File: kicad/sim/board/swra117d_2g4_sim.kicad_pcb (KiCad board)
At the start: 2 copper layers, 40 x 30 mm, 1 part

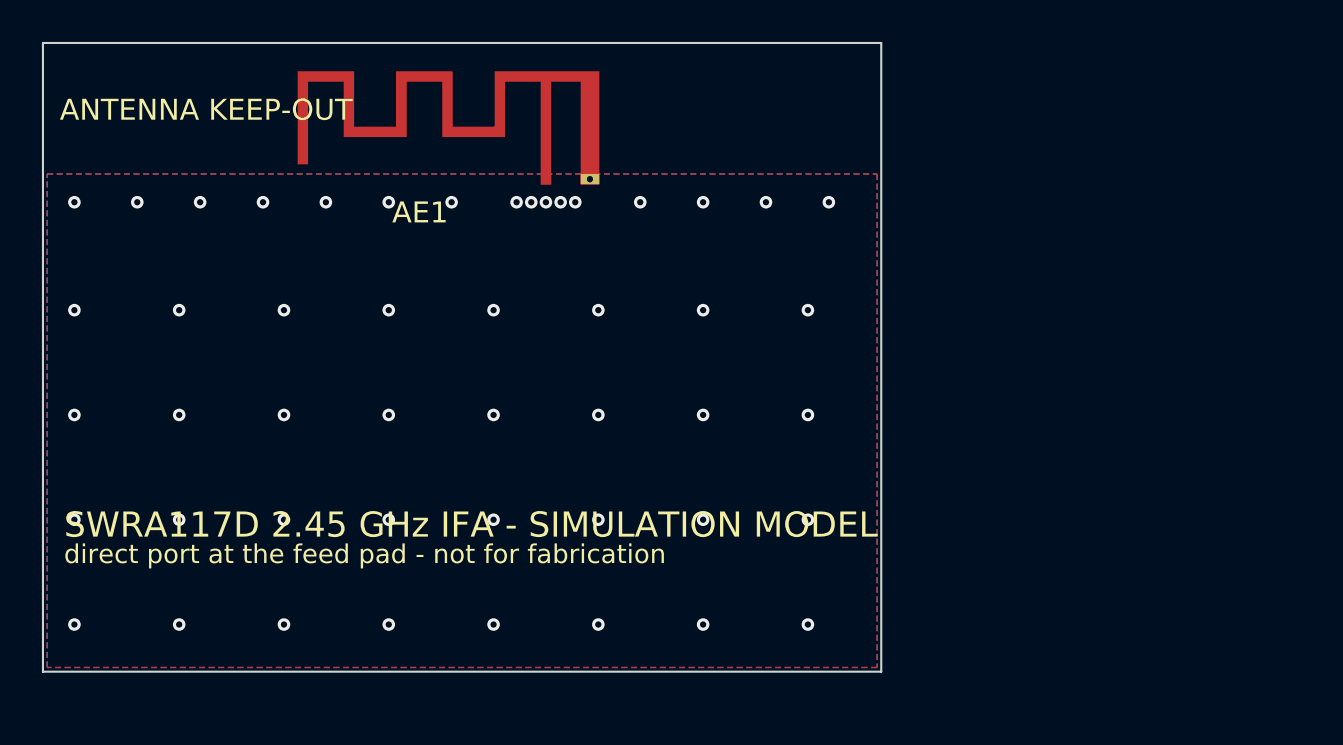
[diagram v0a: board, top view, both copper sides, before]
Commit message: Make the RFsim project a real project: schematic, board, feed - just no SMA
The previous version misread the ask.  "Feed direct, no SMA" meant feed the
antenna directly rather than through a connector, not delete the feed line;
and RFsim is run on a project, so a loose .kicad_pcb with no schematic is not
usable.  Both corrected.

sim/board/swra117d_2g4_sim.{kicad_sch,kicad_pcb,kicad_pro} is now the
fabrication project with exactly one part taken out: J1.  Same antenna file,
same 1.6 mm FR4, same 2.95 mm line and six-step taper, same outline, plane
edge and keep-out.  The line runs to the bottom board edge and stops there,
and that track end is where RFsim attaches port 1.

  * P1 is a new RF_PORT symbol: one passive pin, no footprint, on_board no.
    It marks where the solver drives the line and keeps ERC quiet without
    putting a connector back on the board.
  * Ground vias sit either side of the launch, where the connector's ground
    pads used to be, so the port's return reaches the bottom plane at the
    port.
  * min_copper_edge_clearance is 0 in this project only: a launch belongs on
    the board edge, and that rule exists to protect a board that gets made.

Removing the connector also changes which port model is right, which is the
part that quietly produces a wrong answer: an end-launch footprint makes the
line coplanar, so CPW fits it; with no footprint there is no coplanar ground
and the line is a plain microstrip, so MSL is the match.  Said in the README,
the checklist and the dossier.

gen_sim_board.py imports gen_project.py and reuses its schematic generator,
feed taper, pour rules and board builder, so the two projects cannot drift.
check_sim_board.py now checks the sheet as well as the board - embedded
symbols against the library, every pin on a wire, P1 not placed on the board,
the feed one unbranched run from the board edge to the antenna pad.
mutate_sim_board.py breaks the project 16 ways and catches all 16; a non-zero
exit with no finding is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
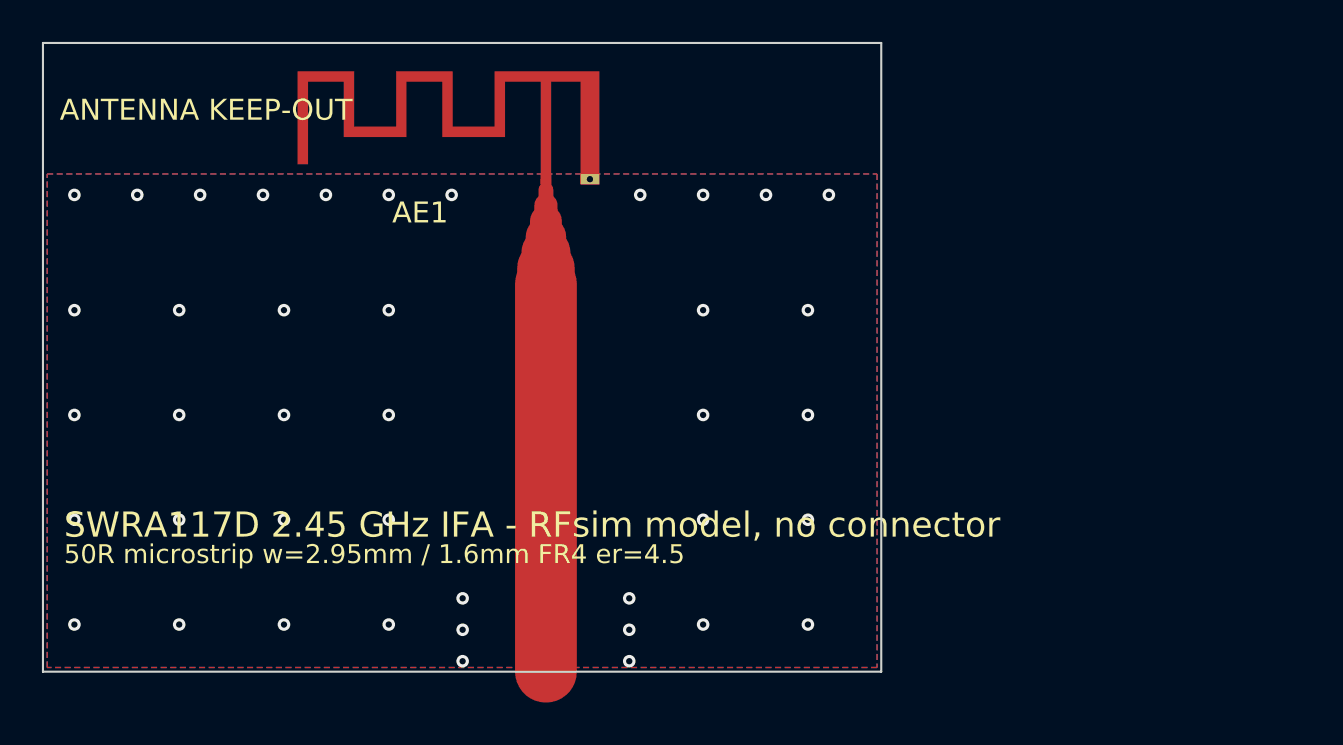
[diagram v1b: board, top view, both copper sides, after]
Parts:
- AE1: value Texas_SWRA117D_2.4GHz_Left -> ANT_SWRA117D_2G4_Left
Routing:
- net ANT_FEED: track 0.00 -> 23.5 mm
- net GND: vias 48 -> 41
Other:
- board text added: "50R microstrip w=2.95mm / 1.6mm FR4 er=4.5"
- board text added: "PORT 1: attach RFsim here, at the track end on the board edge"
- board text added: "SWRA117D 2.45 GHz IFA - RFsim model, no connector"
- board text removed: "PORT 1: 0.4 mm gap, AE1 pad 1 -> GND plane; pour meets the radiator at the short pad only"
- board text removed: "SWRA117D 2.45 GHz IFA - SIMULATION MODEL"
- board text removed: "direct port at the feed pad - not for fabrication"

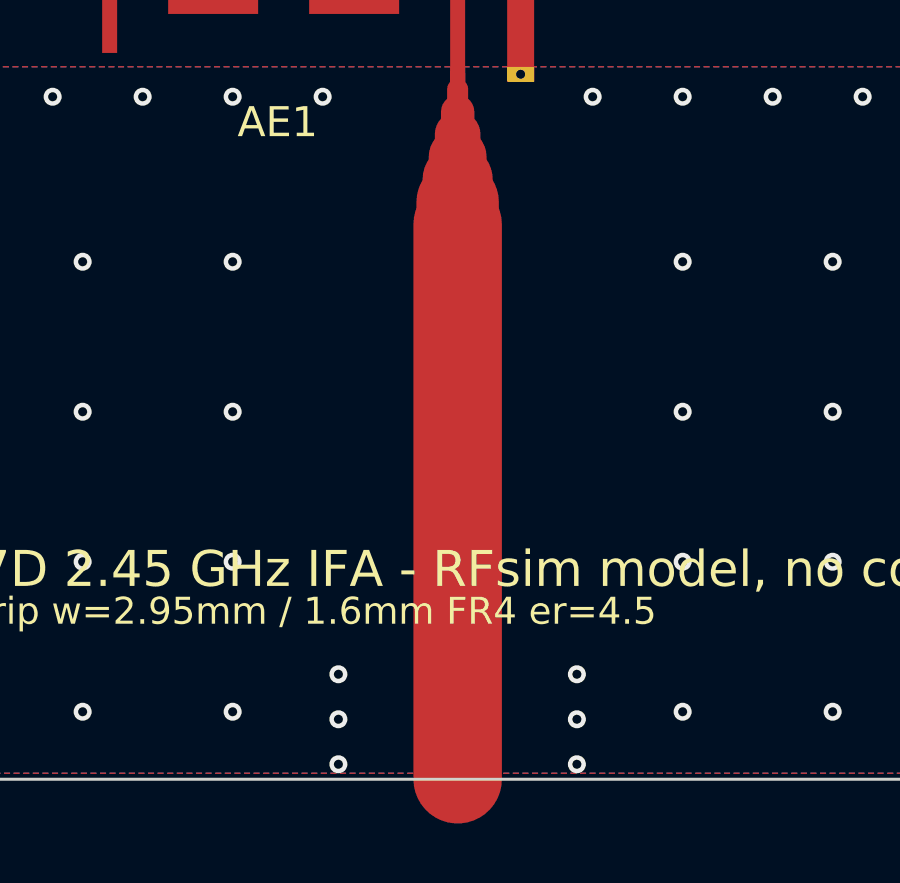
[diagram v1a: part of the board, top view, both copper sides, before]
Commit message: Give the RFsim port a pad with reference copper under it
RFsim reported, on the previous version:

    Port 1 (AE1 Pad 1 (ANT_FEED)): no copper on reference layer B.Cu under
    the pad.

Two things behind it, and the first one was my mistake.  RFsim attaches its
port to a *pad*, not to a track end, so removing the connector left the board
with no pad at the launch and RFsim fell back to the antenna's own feed pad -
which sits on the ground plane edge with the keep-out above it and has no
plane beneath it by design.  A bare track end was never going to work.

So the connector is replaced by a bare port land rather than by nothing:

  * RF_Port_Land - the signal pad, the width of the 50 ohm line, with a solid
    B.Cu ground pad directly under it.  Generated by gen_sma_footprint.py
    --style port, from the same code and the same stackup as the SMA land, so
    the only electrical difference between the two boards is the thing being
    measured.
  * No coplanar ground tabs.  That is what keeps the line a plain microstrip,
    and it is why MSL is the right port model here where CPW is right on the
    fabrication board.  check_sim_board.py fails if anyone adds an F.Cu ground
    pad back, because that silently invalidates the port model the docs tell
    you to use.
  * The reference is a pad, not a zone.  Zones ship unfilled, so a reference
    that waits on a fill is a reference that is missing the first time the
    project is opened - which is the second half of the reported error.

RF_PORT gains a ground pin and the RF_Port_Land footprint; P1 is now a real
board part rather than a sheet-only symbol.  The feed line ends on the port
pad instead of the board edge.  Launch vias sit inside the land's ground pad.

Also fixed: gen_sma_footprint.py derived three uuids from hash(), which
Python salts per process, so the footprint came out different on every run.
Numbered instead.  The fabrication board changes by three uuids and no
geometry.

check_sim_board.py grows t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
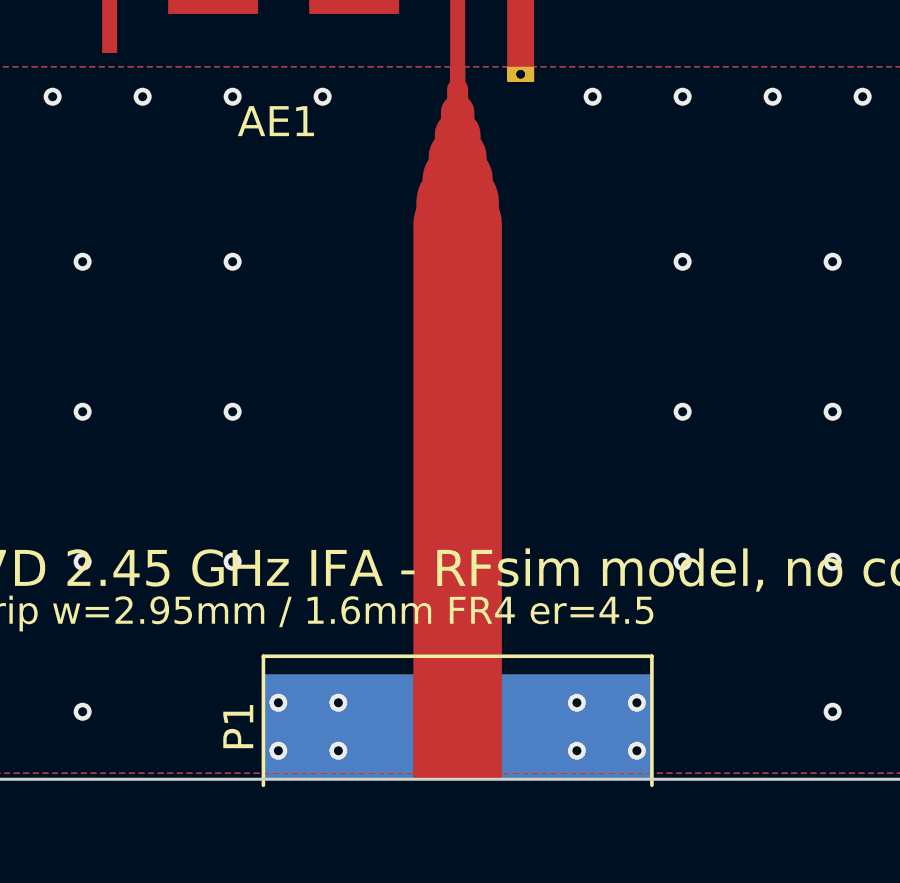
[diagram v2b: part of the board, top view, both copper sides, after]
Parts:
- added P1: 50R port, SWRA117D_RF:RF_Port_Land, F.Cu at (124.0, 90.0)
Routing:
- net ANT_FEED: track 23.5 -> 21.8 mm
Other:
- board text added: "PORT 1: P1 pad 1, referenced to its B.Cu ground pad - microstrip (MSL), not CPW: no coplanar ground here"
- board text removed: "PORT 1: attach RFsim here, at the track end on the board edge"
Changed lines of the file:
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@@
 	(net 1 "GND")
 	(net 2 "ANT_FEED")
+	(footprint "SWRA117D_RF:RF_Port_Land"
+		(layer "F.Cu")
+		(at 124 90 90)
+		(descr "Board-edge port land for a simulator - not a connector. Generated for a 1.6 mm substrate (er 4.5). Pad 1 is the 2.95 mm signal pad the solver drives, the width of the 50 ohm line; pad 2 is the solid ground pad directly under it on B.Cu, so the port has reference copper whether or not the zones are filled. No coplanar ground beside the line, so the line stays a microstrip and a microstrip (MSL) port is the right model."
+		)
+		(tags "RF port land simulation launch 50 ohm microstrip")
+		(attr smd)
+		(property "Reference" "P1"
+			(at 1.75 -7.275 90)
+			(layer "F.SilkS")
+			(effects (font (size 1 1) (thickness 0.15)))
+			(unlocked yes)
+		)
+		(property "Value" "50R port"
+			(at 1.75 7.275 90)
+			(layer "F.Fab")
+			(effects (font (size 1 1) (thickness 0.15)))
+			(unlocked yes)
+		)
+		(fp_text user "%R"
+			(at 1.75 0 90)
+			(layer "F.Fab")
+			(effects (font (size 0.8 0.8) (thickness 0.12)))
+			(unlocked yes)
+		)
+		(fp_line
+			(start -0.2 -6.475)
+			(end 4.1 -6.475)
+			(stroke (width 0.12) (type solid))
+			(layer "F.SilkS")
+		)
+		(fp_line
+			(start -0.2 6.475)
+			(end 4.1 6.475)
+			(stroke (width 0.12) (type solid))
+			(layer "F.SilkS")
+		)
+		(fp_line
+			(start 4.1 -6.475)
+			(end 4.1 6.475)
+			(stroke (width 0.12) (type solid))
+			(layer "F.SilkS")
+		)
+		(fp_line
+			(start -0.2 -6.475)
+			(end 4.1 -6.475)
+			(stroke (width 0.1) (type solid))
+			(layer "F.Fab")
+		)
+		(fp_line
+			(start -0.2 6.475)
+			(end 4.1 6.475)
+			(stroke (width 0.1) (type solid))
+			(layer "F.Fab")
+		)
+		(fp_line
+			(start 4.1 -6.475)
+			(end 4.1 6.475)
+			(stroke (width 0.1) (type solid))
+			(layer "F.Fab")
+		)
+		(fp_rect
+			(start -0.4 -6.675)
+			(end 4.3 6.675)
+			(stroke (width 0.05) (type solid))
+			(fill no)
+			(layer "F.CrtYd")
+		)
+		(fp_rect
+			(start -0.4 -6.675)
+			(end 4.3 6.675)
+			(stroke (width 0.05) (type solid))
+			(fill no)
+			(layer "B.CrtYd")
+		)
+		(pad "1" smd rect
+			(at 1.75 0 90)
+			(size 3.5 2.95)
+			(layers "F.Cu" "F.Paste" "F.Mask")
+			(net 2 "ANT_FEED")
+			(pinfunction "ANT_FEED")
+			(pintype "passive")
+		)
+		(pad "2" smd rect
+			(at 1.75 0 90)
+			(size 3.5 12.95)
+			(layers "B.Cu" "B.Mask")
+			(net 1 "GND")
+			(pinfunction "GND")
+			(pintype "passive")
+		)
+		(sheetname "Root")
+		(sheetfile "swra117d_2g4_sim.kicad_sch")
+		(embedded_fonts no)
+	)
 	(footprint "SWRA117D_RF:Texas_SWRA117D_2.4GHz_Left"
 		(layer "F.Cu")
@@
 	)
 	(segment
-		(start 124 90)
+		(start 124 88.25)
 		(end 124 71.5)
 		(width 2.95)
@@
 	)
 	(via
-		(at 120.025 89.5)
-		(size 0.6)
-		(drill 0.3)
-		(layers "F.Cu" "B.Cu")
-		(net 1)
-	)
-	(via
-		(at 120.025 88)
-		(size 0.6)
-		(drill 0.3)
-		(layers "F.Cu" "B.Cu")
-		(net 1)
-	)
-	(via
-		(at 120.025 86.5)
-		(size 0.6)
-		(drill 0.3)
-		(layers "F.Cu" "B.Cu")
-		(net 1)
-	)
-	(via
-		(at 127.975 89.5)
-		(size 0.6)
-		(drill 0.3)
-		(layers "F.Cu" "B.Cu")
-		(net 1)
-	)
-	(via
-		(at 127.975 88)
-		(size 0.6)
-		(drill 0.3)
-		(layers "F.Cu" "B.Cu")
-		(net 1)
-	)
-	(via
-		(at 127.975 86.5)
+		(at 120.025 87.45)
+		(size 0.6)
+		(drill 0.3)
+		(layers "F.Cu" "B.Cu")
+		(net 1)
+	)
+	(via
+		(at 120.025 89.05)
+		(size 0.6)
+		(drill 0.3)
+		(layers "F.Cu" "B.Cu")
+		(net 1)
+	)
+	(via
+		(at 118.025 87.45)
+		(size 0.6)
+		(drill 0.3)
+		(layers "F.Cu" "B.Cu")
+		(net 1)
+	)
+	(via
+		(at 118.025 89.05)
+		(size 0.6)
+		(drill 0.3)
+		(layers "F.Cu" "B.Cu")
+		(net 1)
+	)
+	(via
+		(at 127.975 87.45)
+		(size 0.6)
+		(drill 0.3)
+		(layers "F.Cu" "B.Cu")
+		(net 1)
+	)
+	(via
+		(at 127.975 89.05)
+		(size 0.6)
+		(drill 0.3)
+		(layers "F.Cu" "B.Cu")
+		(net 1)
+	)
+	(via
+		(at 129.975 87.45)
+		(size 0.6)
+		(drill 0.3)
+		(layers "F.Cu" "B.Cu")
+		(net 1)
+	)
+	(via
+		(at 129.975 89.05)
 		(size 0.6)
 		(drill 0.3)
@@
 	(via
 		(at 111.5 87.75)
-		(size 0.6)
-		(drill 0.3)
-		(layers "F.Cu" "B.Cu")
-		(net 1)
-	)
-	(via
-		(at 116.5 87.75)
-		(size 0.6)
-		(drill 0.3)
-		(layers "F.Cu" "B.Cu")
-		(net 1)
-	)
-	(via
-		(at 131.5 87.75)
 		(size 0.6)
 		(drill 0.3)
@@
 		(effects (font (size 0.9 0.9) (thickness 0.15)) (justify left))
 	)
-	(gr_text "PORT 1: attach RFsim here, at the track end on the board edge"
+	(gr_text "PORT 1: P1 pad 1, referenced to its B.Cu ground pad - microstrip (MSL), not CPW: no coplanar ground here"
 		(at 100.8 89 0)
 		(layer "Cmts.User")
